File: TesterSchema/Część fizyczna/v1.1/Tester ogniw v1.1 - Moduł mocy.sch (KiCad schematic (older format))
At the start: 46 parts, among them J1 J2, K1 K10, K3 Zasilanie, K4 Badany AKU, T1 IRFP9140, T2 IRFP054N, T3 BC547, T4 BC547, T5 T_PNP, T6 BC547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

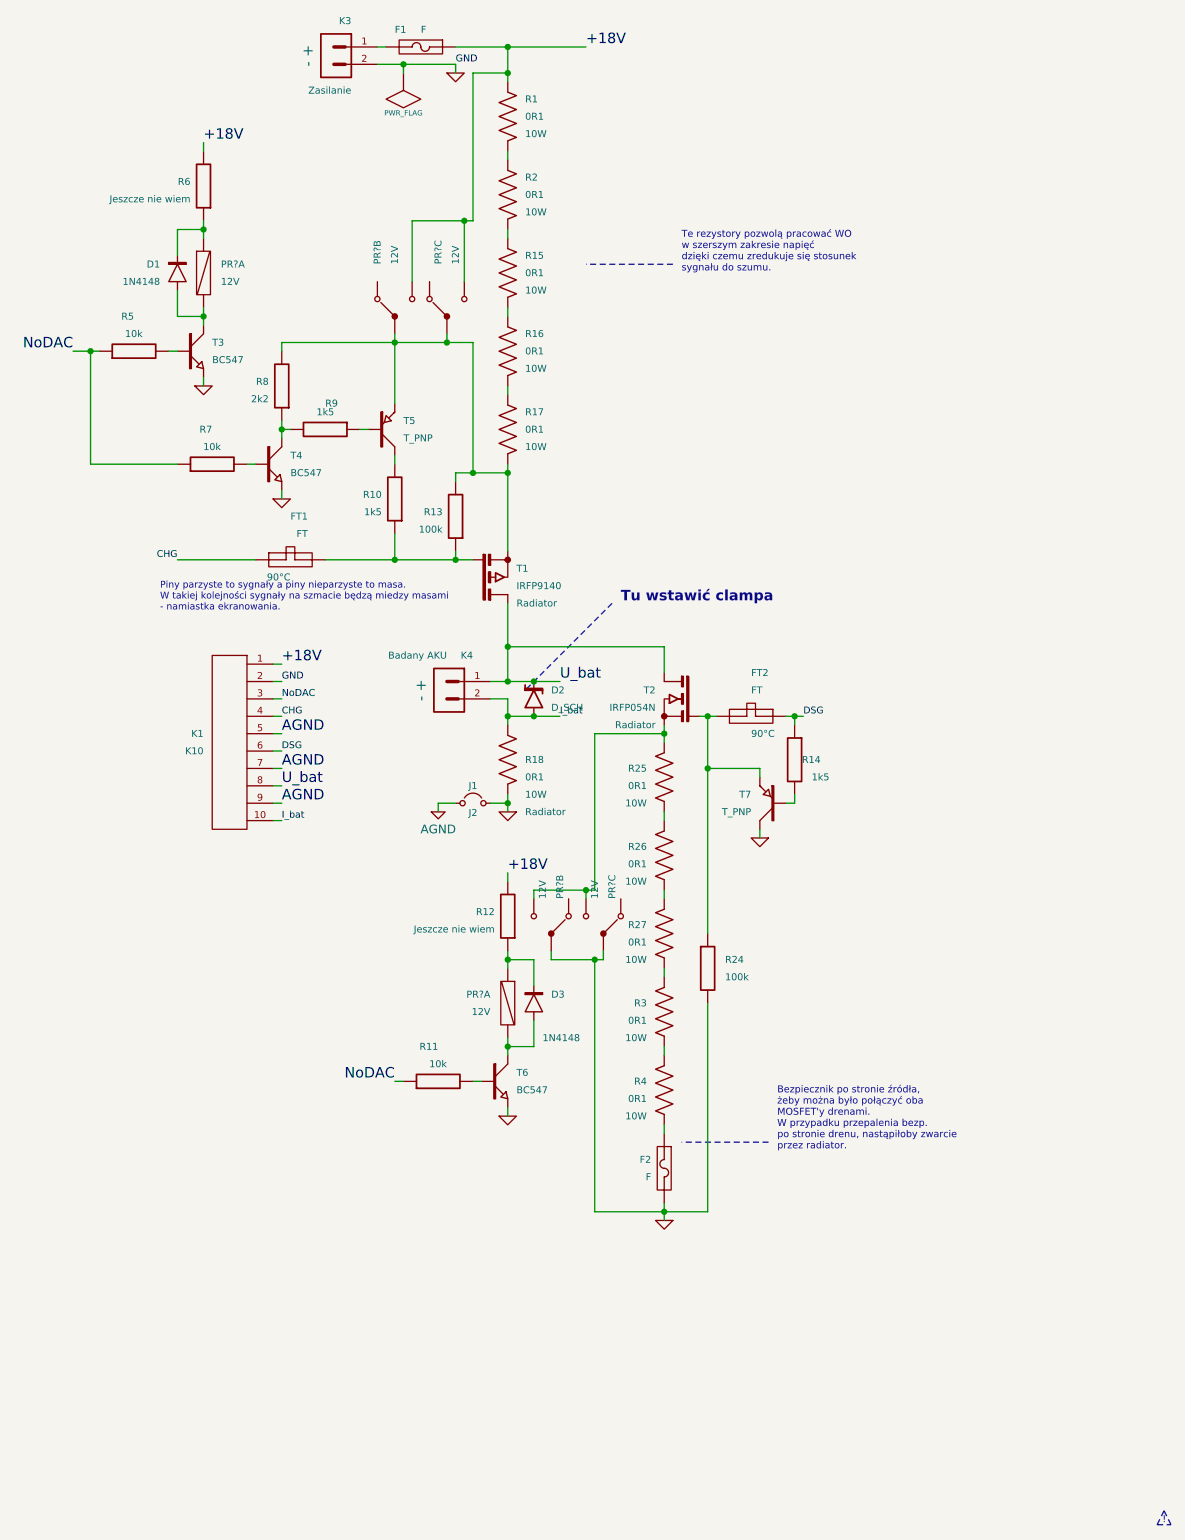
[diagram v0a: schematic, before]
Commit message: Poprawienie schematu Sterownika w związku z migracją na KiCAD2015 Poprawienie schematu Modułu Mocy w związku z migracją na KiCAD2015 i dodaniem clamp'a na wyjściu AKU
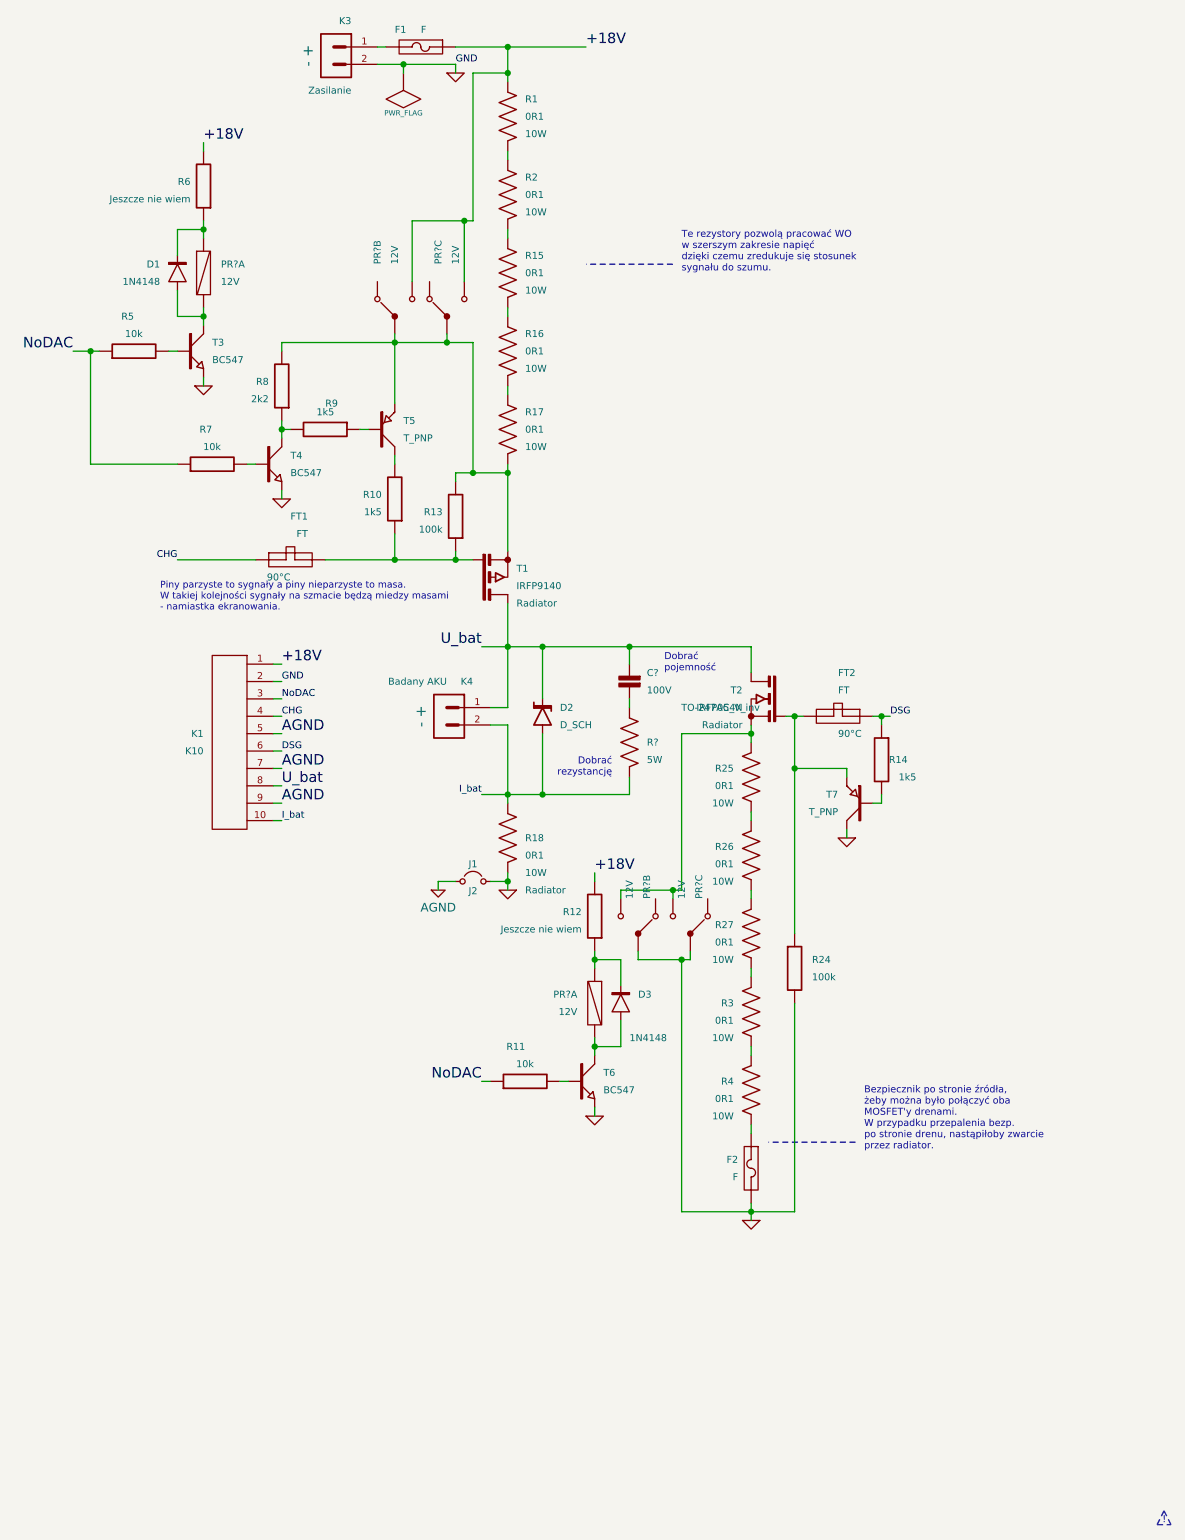
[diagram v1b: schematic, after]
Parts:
- added C?: 100V, symbol C
- added R?: 5W, symbol R_MOCY
- D1, D3: footprint (none) -> DO-35
- D2: footprint (none) -> Modele:DO-8
- F1, F2: footprint (none) -> Modele:BEZP-19MM-AMFGN
- FT1, FT2: footprint (none) -> Modele:PIN-2-I
- J1: footprint (none) -> bridge_3mm
- K1: footprint (none) -> IDE-V-10
- K3, K4: footprint (none) -> ark500-2
- R1, R15, R16, R17, R2, R25, R26, R27, R3, R4: footprint (none) -> resistor-10W_9x49
- R10, R11, R13, R14, R5, R7, R8, R9: footprint (none) -> 7:
- R12, R24, R6: footprint (none) -> 10:
- R18: footprint (none) -> resistor-25W_17x29
- T1: footprint (none) -> TO-247AC_V_inv
- T2: footprint ~ -> TO-247AC_V_inv
- T3, T4, T5, T6, T7: footprint (none) -> Modele:TO-92-B
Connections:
- net I_bat: now also R?.2
- net U_bat: now also C?.1
- new net: C?.2, R?.1
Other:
- note added: "Dobrać\npojemność"
- note added: "Dobrać\nrezystancję"
- note removed: "Tu wstawić clampa"
- moved on the sheet: D2, D3, F2, FT2, J1, K4, PR?A, PR?B, PR?C, R11, R12, R14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

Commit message: Naprawa repo
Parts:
- R10, R11, R13, R14, R5, R7, R8, R9: footprint 7: -> resistor-0207_7
- R12, R24, R6: footprint 10: -> resistor-0207_10
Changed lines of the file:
@@
 F 0 "R24" H 9550 7850 40  0000 L CNN
 F 1 "100k" H 9550 7750 40  0000 L CNN
-F 2 "10:" H 9450 7800 60  0001 C CNN
+F 2 "resistor-0207_10" H 9450 7800 60  0001 C CNN
 F 3 "" H 9450 7800 60  0001 C CNN
 	1    9450 7800
@@
 F 0 "R13" H 7575 5175 40  0000 L CNN
 F 1 "100k" H 7575 5275 40  0000 L CNN
-F 2 "7:" H 7500 5200 60  0001 C CNN
+F 2 "resistor-0207_7" H 7500 5200 60  0001 C CNN
 F 3 "" H 7500 5200 60  0001 C CNN
 	1    7500 5200
@@
 F 0 "R5" V 5850 4250 40  0000 L CNN
 F 1 "10k" V 5750 4200 40  0000 L CNN
-F 2 "7:" H 5650 4250 60  0001 C CNN
+F 2 "resistor-0207_7" H 5650 4250 60  0001 C CNN
 F 3 "" H 5650 4250 60  0001 C CNN
 	1    5650 4250
@@
 F 0 "R11" V 8100 8450 40  0000 L CNN
 F 1 "10k" V 8000 8400 40  0000 L CNN
-F 2 "7:" H 7900 8450 60  0001 C CNN
+F 2 "resistor-0207_7" H 7900 8450 60  0001 C CNN
 F 3 "" H 7900 8450 60  0001 C CNN
 	1    7900 8450
@@
 F 0 "R12" H 8375 7475 40  0000 L CNN
 F 1 "Jeszcze nie wiem" H 8375 7575 40  0000 L CNN
-F 2 "10:" H 8300 7500 60  0001 C CNN
+F 2 "resistor-0207_10" H 8300 7500 60  0001 C CNN
 F 3 "" H 8300 7500 60  0001 C CNN
 	1    8300 7500
@@
 F 0 "R6" H 6125 3275 40  0000 L CNN
 F 1 "Jeszcze nie wiem" H 6125 3375 40  0000 L CNN
-F 2 "10:" H 6050 3300 60  0001 C CNN
+F 2 "resistor-0207_10" H 6050 3300 60  0001 C CNN
 F 3 "" H 6050 3300 60  0001 C CNN
 	1    6050 3300
@@
 F 0 "R7" V 6300 4900 40  0000 L CNN
 F 1 "10k" V 6200 4850 40  0000 L CNN
-F 2 "7:" H 6100 4900 60  0001 C CNN
+F 2 "resistor-0207_7" H 6100 4900 60  0001 C CNN
 F 3 "" H 6100 4900 60  0001 C CNN
 	1    6100 4900
@@
 F 0 "R8" H 6575 4425 40  0000 L CNN
 F 1 "2k2" H 6575 4525 40  0000 L CNN
-F 2 "7:" H 6500 4450 60  0001 C CNN
+F 2 "resistor-0207_7" H 6500 4450 60  0001 C CNN
 F 3 "" H 6500 4450 60  0001 C CNN
 	1    6500 4450
@@
 F 0 "R9" V 6600 4700 40  0000 L CNN
 F 1 "1k5" V 6650 4650 40  0000 L CNN
-F 2 "7:" H 6750 4700 60  0001 C CNN
+F 2 "resistor-0207_7" H 6750 4700 60  0001 C CNN
 F 3 "" H 6750 4700 60  0001 C CNN
 	1    6750 4700
@@
 F 0 "R10" H 7225 5075 40  0000 L CNN
 F 1 "1k5" H 7225 5175 40  0000 L CNN
-F 2 "7:" H 7150 5100 60  0001 C CNN
+F 2 "resistor-0207_7" H 7150 5100 60  0001 C CNN
 F 3 "" H 7150 5100 60  0001 C CNN
 	1    7150 5100
@@
 F 0 "R14" H 9800 6600 40  0000 L CNN
 F 1 "1k5" H 9750 6500 40  0000 L CNN
-F 2 "7:" H 9950 6600 60  0001 C CNN
+F 2 "resistor-0207_7" H 9950 6600 60  0001 C CNN
 F 3 "" H 9950 6600 60  0001 C CNN
 	1    9950 6600
